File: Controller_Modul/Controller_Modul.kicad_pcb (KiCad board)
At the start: 4 copper layers, 78 x 100 mm, 138 parts, among them J101 Screw_Terminal_01x06, J102 Conn_02x01, J103 Conn_01x06_Male, J104 Conn_02x01, J105 Conn_01x04_Male, J106 Conn_01x08_Male, J107 Micro_SD_Card_Det, J108 Conn_02x07_Odd_Even, J109 Conn_02x20_Odd_Even, J110 USB_B_Mini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

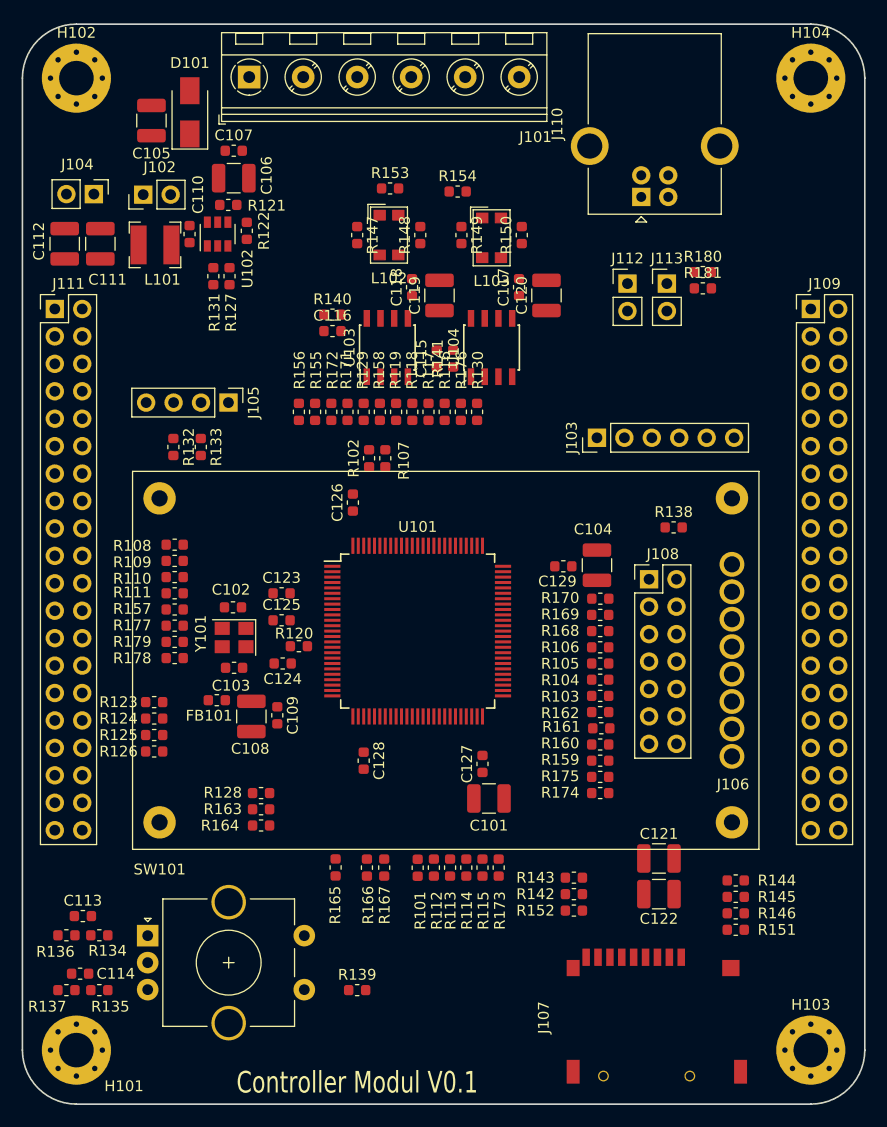
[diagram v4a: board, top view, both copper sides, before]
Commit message: Controller Modul geroutet
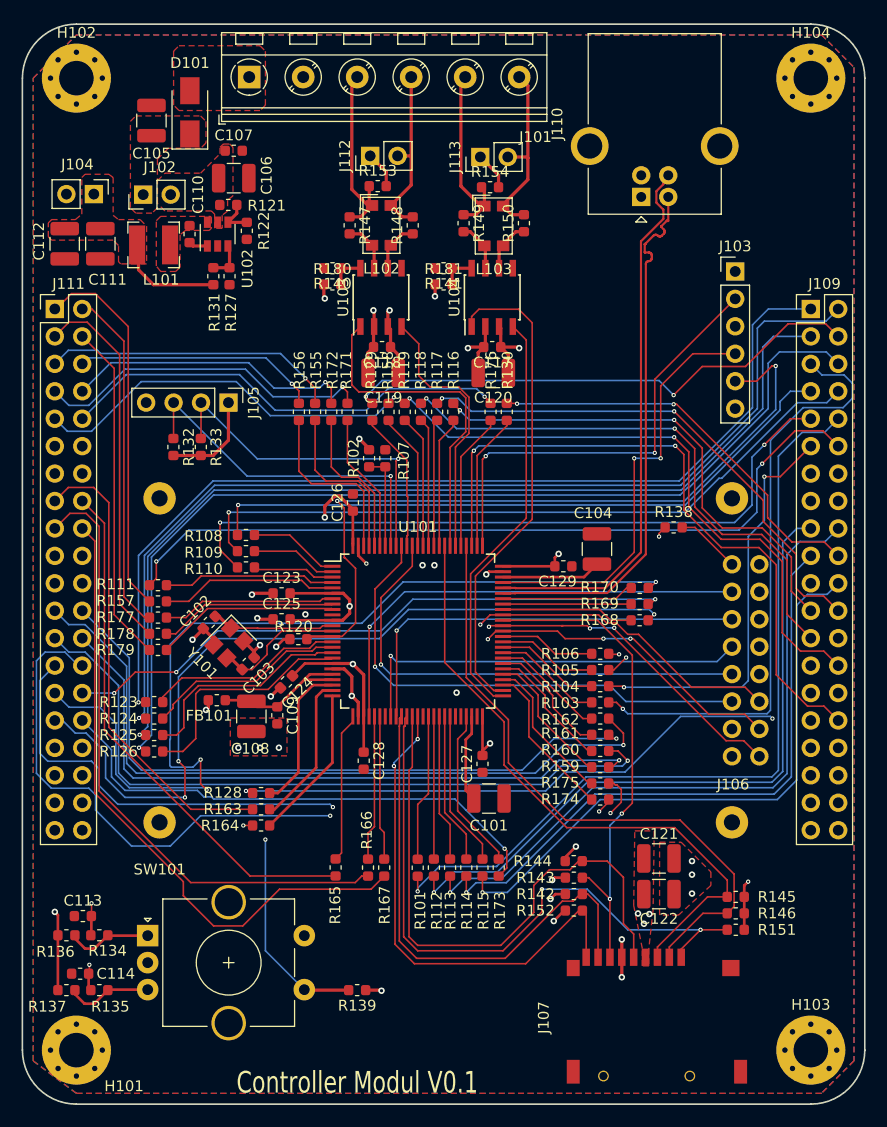
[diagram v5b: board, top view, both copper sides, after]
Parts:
- removed C115, C116: 100n, Capacitor_SMD:C_0603_1608Metric
- removed J108: Conn_02x07_Odd_Even, Connector_PinHeader_2.54mm:PinHeader_2x07_P2.54mm_Vertical
- J106: footprint ProjectFootprints:ST7789_Waveshare -> ProjectFootprints:ST7789_Waveshare2
- R140, R141: value 10K -> 1K
- moved R180 34.3 mm to (108.7, 74.1)
- moved J112 26.6 mm to (112.2, 62.2), turned to 90 degrees
- moved R181 24.0 mm to (119.0, 74.1)
- moved J113 20.9 mm to (122.4, 62.3), turned to 90 degrees
- moved J103 20.0 mm to (146.0, 72.9), turned to 0 degrees
- moved R144 15.1 mm to (131.1, 127.5), turned to 180 degrees
- moved C119 8.88 mm to (113.4, 82.3), turned to 180 degrees
- moved C120 8.71 mm to (123.6, 82.3), turned to 180 degrees
- moved R141 8.41 mm to (119.0, 72.6), turned to 180 degrees
- moved R108 6.66 mm to (100.7, 97.3)
- moved R109 6.66 mm to (100.7, 98.8)
- moved R110 6.66 mm to (100.7, 100.3)
- moved C118 6.20 mm to (113.3, 79.9), turned to 180 degrees
- moved C117 6.07 mm to (123.5, 79.9), turned to 180 degrees
- moved U103 4.68 mm to (113.2, 75.3)
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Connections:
- J110 pad 2: /PA12 -> /USB_FS_D-
- J110 pad 3: /PA11 -> /USB_FS_D+
- U101 pad 70: /PA11 -> /USB_FS_D-
- U101 pad 71: /PA12 -> /USB_FS_D+
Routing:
- net +3V3: track 0.00 -> 94.3 mm, vias 0 -> 22
- net /DIAG_ROT: track 0.00 -> 94.0 mm, vias 0 -> 1
- net /DIR_ROT: track 0.00 -> 93.3 mm, vias 0 -> 1
- net /INDEX_ROT: track 0.00 -> 90.6 mm, vias 0 -> 1
- net /EN_ROT: track 0.00 -> 90.5 mm, vias 0 -> 1
- net /OUTPUT_RES4: track 0.00 -> 86.3 mm, vias 0 -> 3
- net /PC6: track 0.00 -> 83.2 mm, vias 0 -> 4
- net /PC7: track 0.00 -> 80.7 mm, vias 0 -> 4
- net /OUTPUT_RES3: track 0.00 -> 77.5 mm, vias 0 -> 2
- net /ENC_BTN: track 0.00 -> 77.2 mm, vias 0 -> 2
- net /STEP_Z: track 0.00 -> 75.7 mm, vias 0 -> 1
- net /OUTPUT_RES6: track 0.00 -> 75.4 mm, vias 0 -> 3
- net /DIR_Z: track 0.00 -> 73.5 mm, vias 0 -> 2
- net /NRST: track 0.00 -> 69.7 mm, vias 0 -> 2
- net /VENTIL1: track 0.00 -> 68.2 mm, vias 0 -> 1
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- added copper zone on F.Cu, net +24V
- added copper zone on F.Cu, net +3V3
- added copper zone on In1.Cu, net +3V3
- added copper zone on B.Cu, net GND
- added copper zone on F.Cu, net GND
- added copper zone on In2.Cu, net GND
- added copper zone on F.Cu, net Net-(C106-Pad1)
- added copper zone on F.Cu, net Net-(C110-Pad1)
- added copper zone on F.Cu, net Net-(C111-Pad1)
- added copper zone on F.Cu, net Net-(D101-Pad2)
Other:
- net class USB_90Ohm added: clearance 0.15, trace_width 0.15, via_dia 0.4, via_drill 0.2

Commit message: display modul fertig
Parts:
- added U105: SRV05-4, Package_TO_SOT_SMD:SOT-23-6, F.Cu at (133.6, 72.0)
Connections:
- J106 pad 10: GND -> /PC6
- J106 pad 11: GND -> /ENC_BTN
- J106 pad 14: /ENC_BTN -> GND
- J106 pad 15: /PC6 -> GND
- J106 pad 16: /PC7 -> GND
- J106 pad 9: GND -> /PC7
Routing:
- net /USB_FS_D-: track 50.4 -> 63.2 mm, vias 0 -> 1
- net /PB0: track 47.7 -> 59.7 mm
- net /PB2: track 54.0 -> 65.4 mm
- net /PE7: track 46.7 -> 57.4 mm
- net /USB_FS_D+: track 50.7 -> 61.2 mm, vias 0 -> 1
- net /ADC_RES4: track 59.6 -> 53.0 mm
- net /ADC_RES3: track 58.3 -> 55.3 mm
- net /PD2: track 58.5 -> 61.0 mm
- net /PC7: track 80.7 -> 78.3 mm
- net /PC11: track 58.4 -> 60.7 mm
- net /PC6: track 83.2 -> 85.3 mm
- net +3V3: track 94.3 -> 95.9 mm, vias 22 -> 24
- net /ENC_BTN: track 77.2 -> 76.3 mm
- net /PC3: track 21.7 -> 20.9 mm
- net /STEP_Y: track 63.4 -> 64.2 mm
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
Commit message: Leere Symbole mit leeren Footprints hinzugefügt für BOM export
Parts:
- added J108: IPC 16P, ProjectFootprints:Empty, F.Cu at (152.0, 60.0)
- added J114: IPC 40P, ProjectFootprints:Empty, F.Cu at (154.0, 60.0)
- added J115: IPC 40P, ProjectFootprints:Empty, F.Cu at (150.0, 60.0)
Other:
- board text added: "Empty Footprints IDC- Connector for BOM"

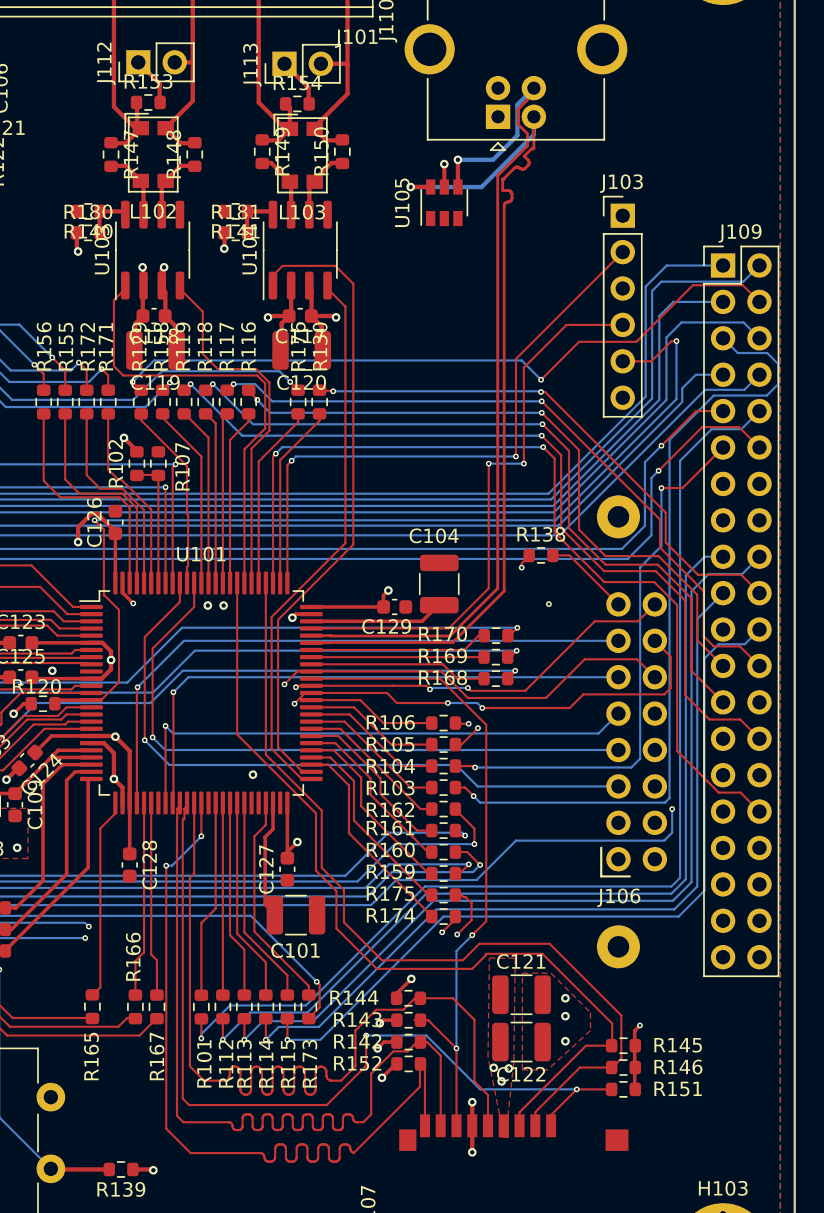
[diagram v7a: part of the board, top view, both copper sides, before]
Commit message: CV Modul Reset Button hinzugefügt
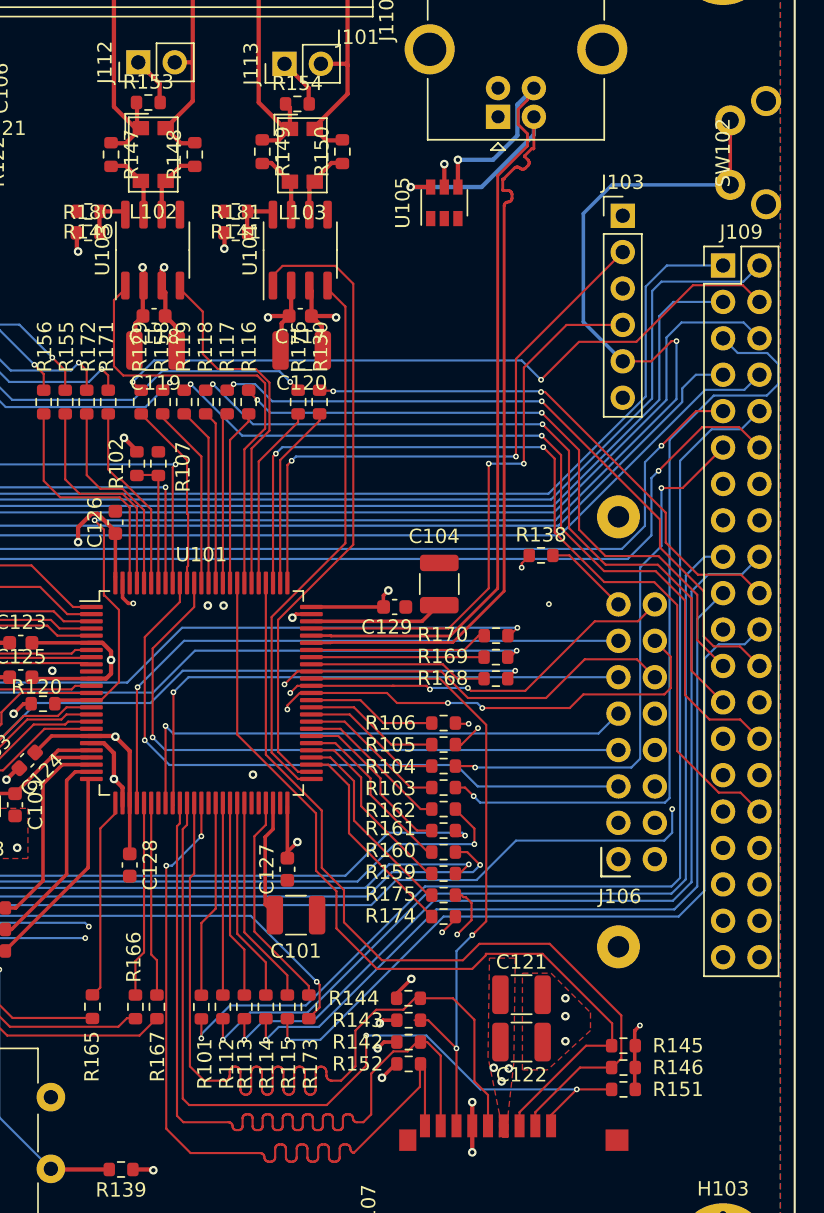
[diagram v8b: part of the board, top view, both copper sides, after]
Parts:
- added SW102: SW_Push, ProjectFootprints:TactileSwitchLCSC, F.Cu at (153.5, 68.5)
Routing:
- net /NRST: track 69.7 -> 96.7 mm
- net /PC6: track 85.3 -> 83.3 mm
